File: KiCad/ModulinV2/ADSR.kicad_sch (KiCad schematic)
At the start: 65 parts, among them IC48 TL074HIDR, IC49 AS3310D, IC50 AS3310D

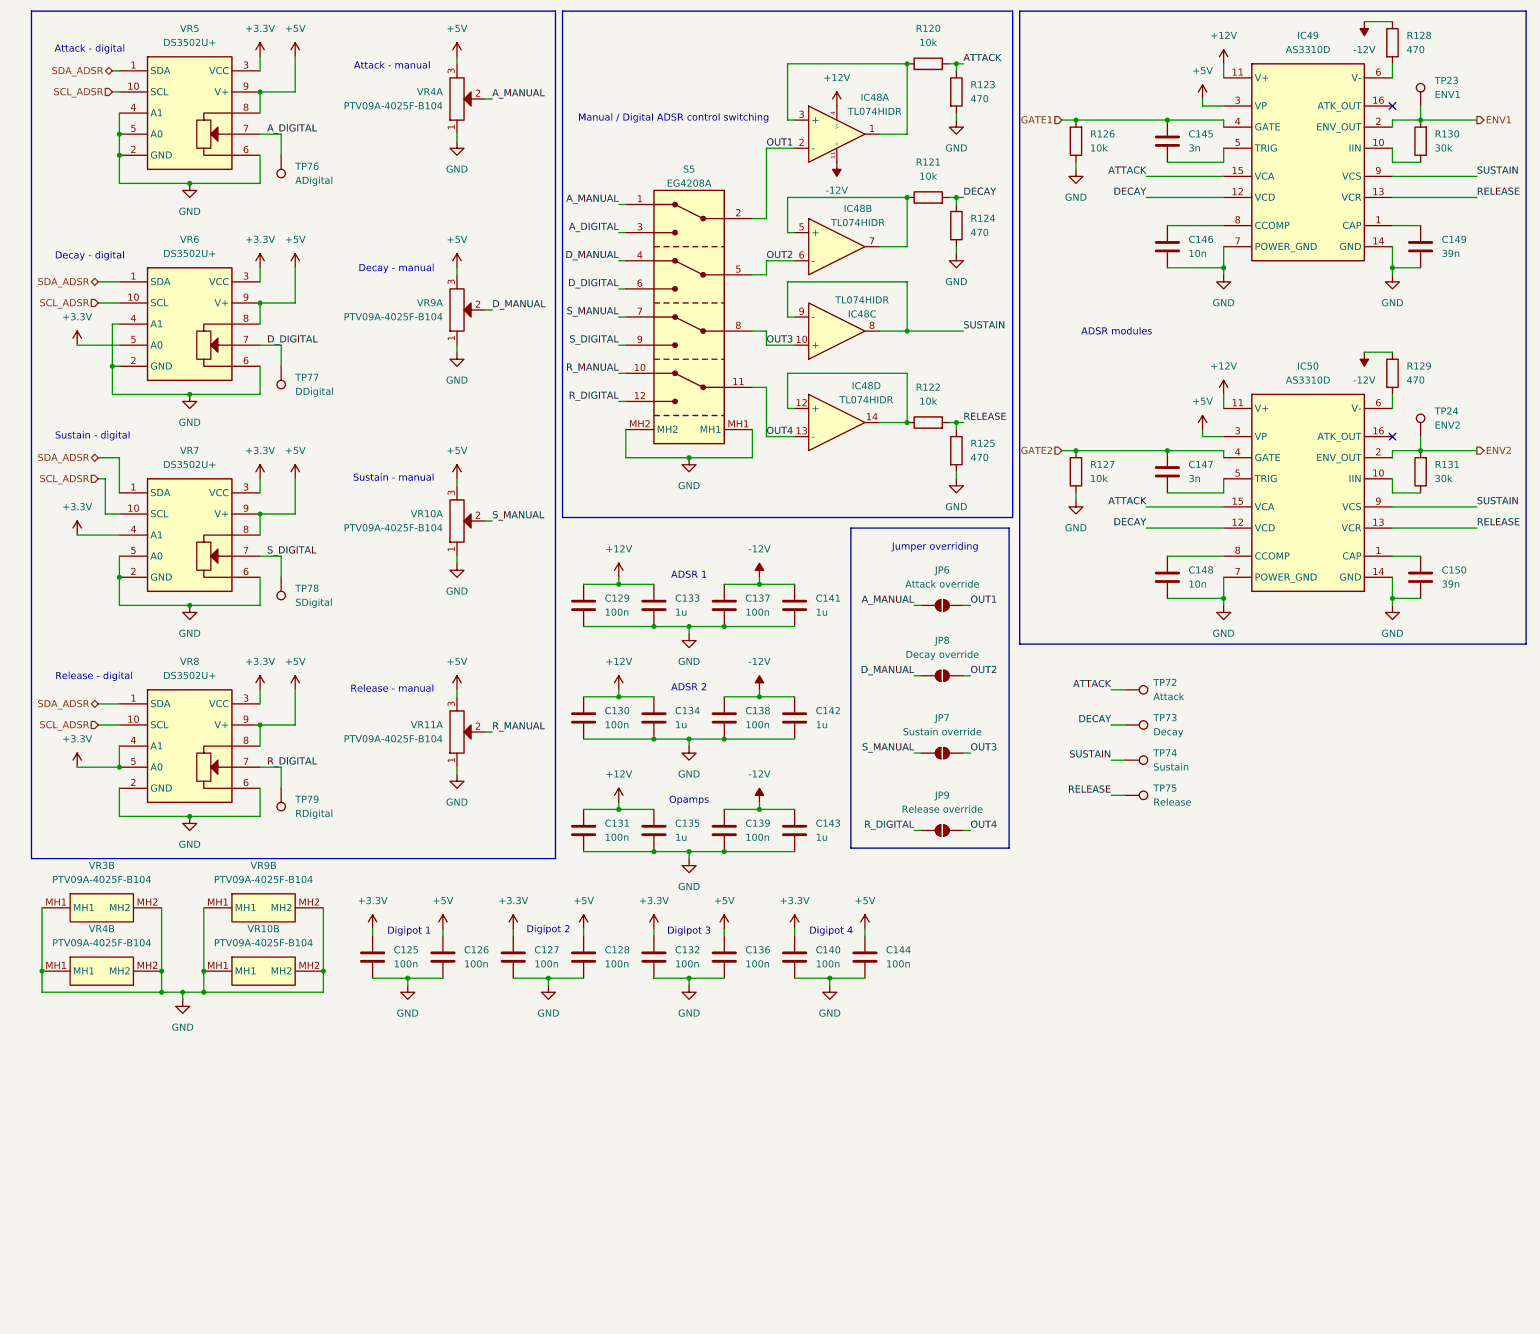
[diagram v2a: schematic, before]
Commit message: Added footprints to all capacitors and potentiometers
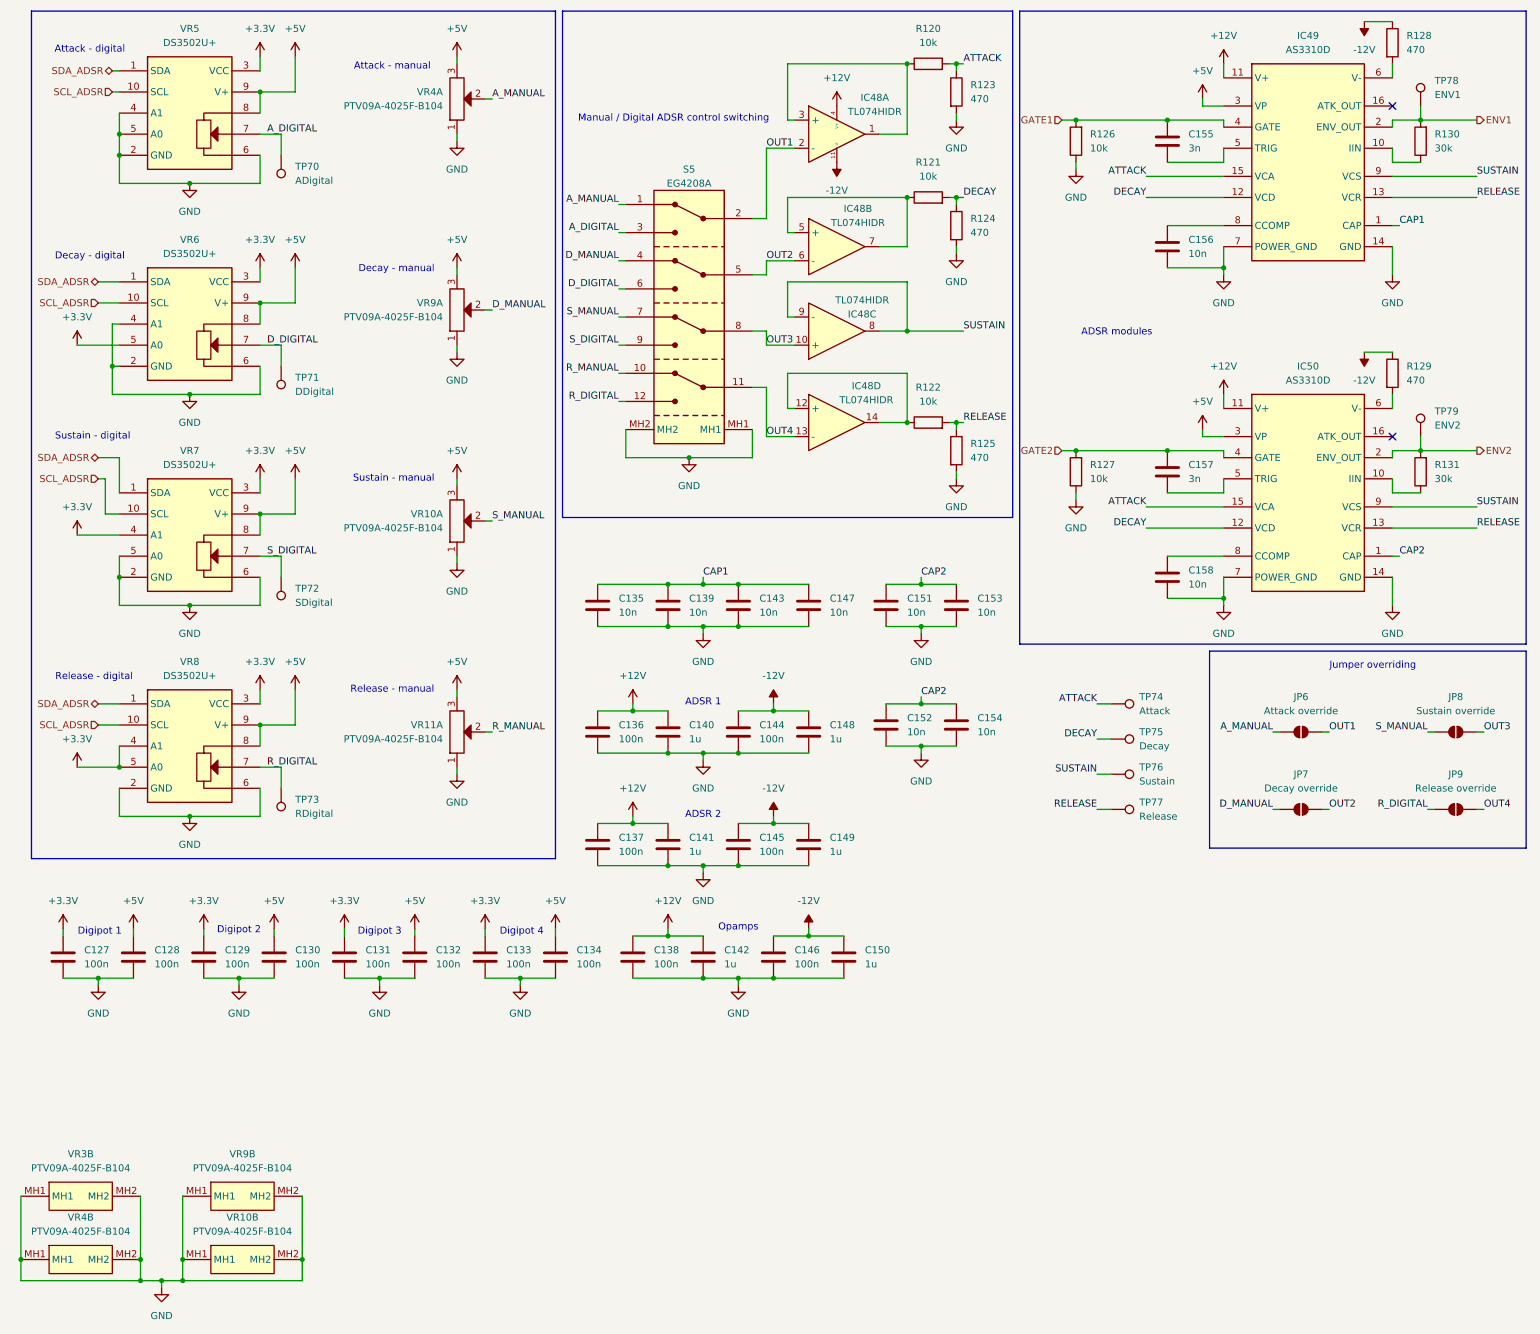
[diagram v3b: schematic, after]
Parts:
- removed C149, C150: 39n, symbol Device:C
- added C135, C139, C143, C147, C151, C152, C153, C154: 10n, Capacitor_SMD:C_0603_1608Metric_Pad1.08x0.95mm_HandSolder, symbol Device:C
- C127: renamed from C125; footprint SamacSys_Parts:CAPC1608X90N -> Capacitor_SMD:C_0603_1608Metric_Pad1.08x0.95mm_HandSolder
- C128: renamed from C126; footprint SamacSys_Parts:CAPC1608X90N -> Capacitor_SMD:C_0603_1608Metric_Pad1.08x0.95mm_HandSolder
- C129: renamed from C127; footprint SamacSys_Parts:CAPC1608X90N -> Capacitor_SMD:C_0603_1608Metric_Pad1.08x0.95mm_HandSolder
- C130: renamed from C128; footprint SamacSys_Parts:CAPC1608X90N -> Capacitor_SMD:C_0603_1608Metric_Pad1.08x0.95mm_HandSolder
- C131: renamed from C132; footprint SamacSys_Parts:CAPC1608X90N -> Capacitor_SMD:C_0603_1608Metric_Pad1.08x0.95mm_HandSolder
- C132: renamed from C136; footprint SamacSys_Parts:CAPC1608X90N -> Capacitor_SMD:C_0603_1608Metric_Pad1.08x0.95mm_HandSolder
- C133: renamed from C140; footprint SamacSys_Parts:CAPC1608X90N -> Capacitor_SMD:C_0603_1608Metric_Pad1.08x0.95mm_HandSolder
- C134: renamed from C144; footprint SamacSys_Parts:CAPC1608X90N -> Capacitor_SMD:C_0603_1608Metric_Pad1.08x0.95mm_HandSolder
- C136: renamed from C129; footprint SamacSys_Parts:CAPC1608X90N -> Capacitor_SMD:C_0603_1608Metric_Pad1.08x0.95mm_HandSolder
- C137: renamed from C130; footprint SamacSys_Parts:CAPC1608X90N -> Capacitor_SMD:C_0603_1608Metric_Pad1.08x0.95mm_HandSolder
- C138: renamed from C131; footprint SamacSys_Parts:CAPC1608X90N -> Capacitor_SMD:C_0603_1608Metric_Pad1.08x0.95mm_HandSolder
- C140: renamed from C133; footprint SamacSys_Parts:CAPC1608X95N -> Capacitor_SMD:C_0603_1608Metric_Pad1.08x0.95mm_HandSolder
- C141: renamed from C134; footprint SamacSys_Parts:CAPC1608X95N -> Capacitor_SMD:C_0603_1608Metric_Pad1.08x0.95mm_HandSolder
- C142: renamed from C135; footprint SamacSys_Parts:CAPC1608X95N -> Capacitor_SMD:C_0603_1608Metric_Pad1.08x0.95mm_HandSolder
- C144: renamed from C137; footprint SamacSys_Parts:CAPC1608X90N -> Capacitor_SMD:C_0603_1608Metric_Pad1.08x0.95mm_HandSolder
- C145: renamed from C138; footprint SamacSys_Parts:CAPC1608X90N -> Capacitor_SMD:C_0603_1608Metric_Pad1.08x0.95mm_HandSolder
- C146: renamed from C139; footprint SamacSys_Parts:CAPC1608X90N -> Capacitor_SMD:C_0603_1608Metric_Pad1.08x0.95mm_HandSolder
- C148: renamed from C141; footprint SamacSys_Parts:CAPC1608X95N -> Capacitor_SMD:C_0603_1608Metric_Pad1.08x0.95mm_HandSolder
- C149: renamed from C142; footprint SamacSys_Parts:CAPC1608X95N -> Capacitor_SMD:C_0603_1608Metric_Pad1.08x0.95mm_HandSolder
- C150: renamed from C143; footprint SamacSys_Parts:CAPC1608X95N -> Capacitor_SMD:C_0603_1608Metric_Pad1.08x0.95mm_HandSolder
- C155: renamed from C145; footprint (none) -> Capacitor_SMD:C_0603_1608Metric_Pad1.08x0.95mm_HandSolder
- C156: renamed from C146; footprint SamacSys_Parts:CAPC1608X90N -> Capacitor_SMD:C_0603_1608Metric_Pad1.08x0.95mm_HandSolder
- C157: renamed from C147; footprint (none) -> Capacitor_SMD:C_0603_1608Metric_Pad1.08x0.95mm_HandSolder
- C158: renamed from C148; footprint SamacSys_Parts:CAPC1608X90N -> Capacitor_SMD:C_0603_1608Metric_Pad1.08x0.95mm_HandSolder
- renumbered JP8 to JP7, JP7 to JP8, TP76 to TP70, TP77 to TP71, TP78 to TP72, TP79 to TP73, TP72 to TP74, TP73 to TP75, TP74 to TP76, TP75 to TP77, TP23 to TP78, TP24 to TP79
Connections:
- net GND: now also C135.2, C139.2, C143.2, C147.2, C151.2, C152.2, C153.2, C154.2
- net CAP1: now reaches IC49.1 (CAP)
- net CAP1: now also C135.1, C139.1, C143.1, C147.1
- net CAP2: now reaches IC50.1 (CAP)
- net CAP2: now also C151.1, C152.1, C153.1, C154.1
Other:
- moved on the sheet: C127, C128, C129, C130, C131, C132, C133, C134, C136, C137, C138, C140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

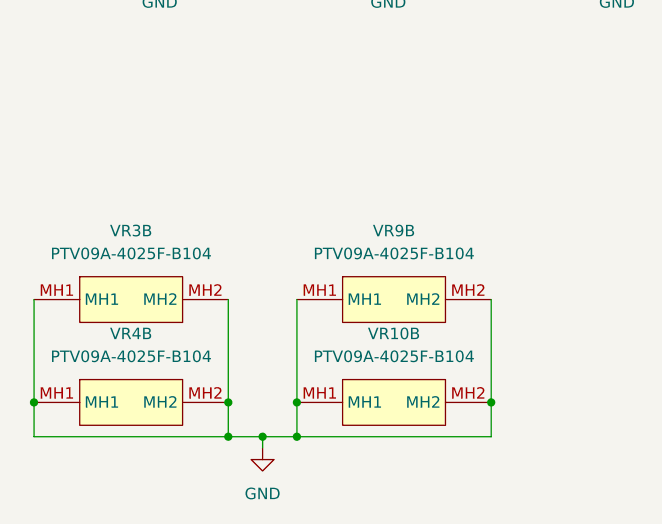
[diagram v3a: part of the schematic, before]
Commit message: Made LFO and VCF schematics in addition to making a better reference voltage supply
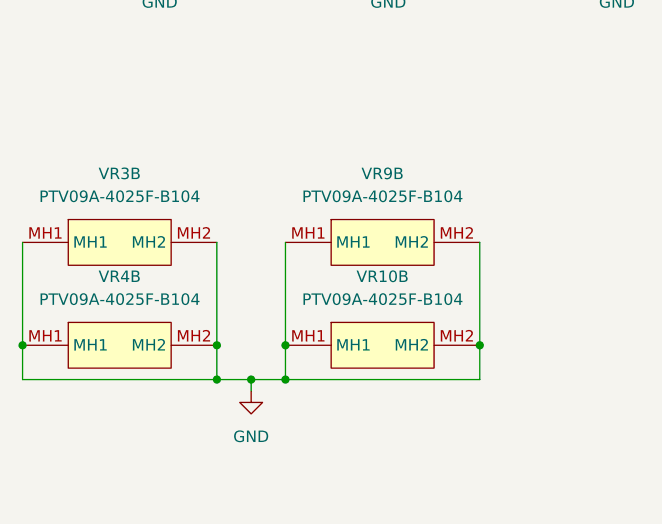
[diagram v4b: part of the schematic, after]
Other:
- moved on the sheet: VR10B, VR3B, VR4B, VR9B
